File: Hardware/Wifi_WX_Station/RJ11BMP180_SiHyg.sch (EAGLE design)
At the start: 8 parts, among them U1 SI7021-DFN6

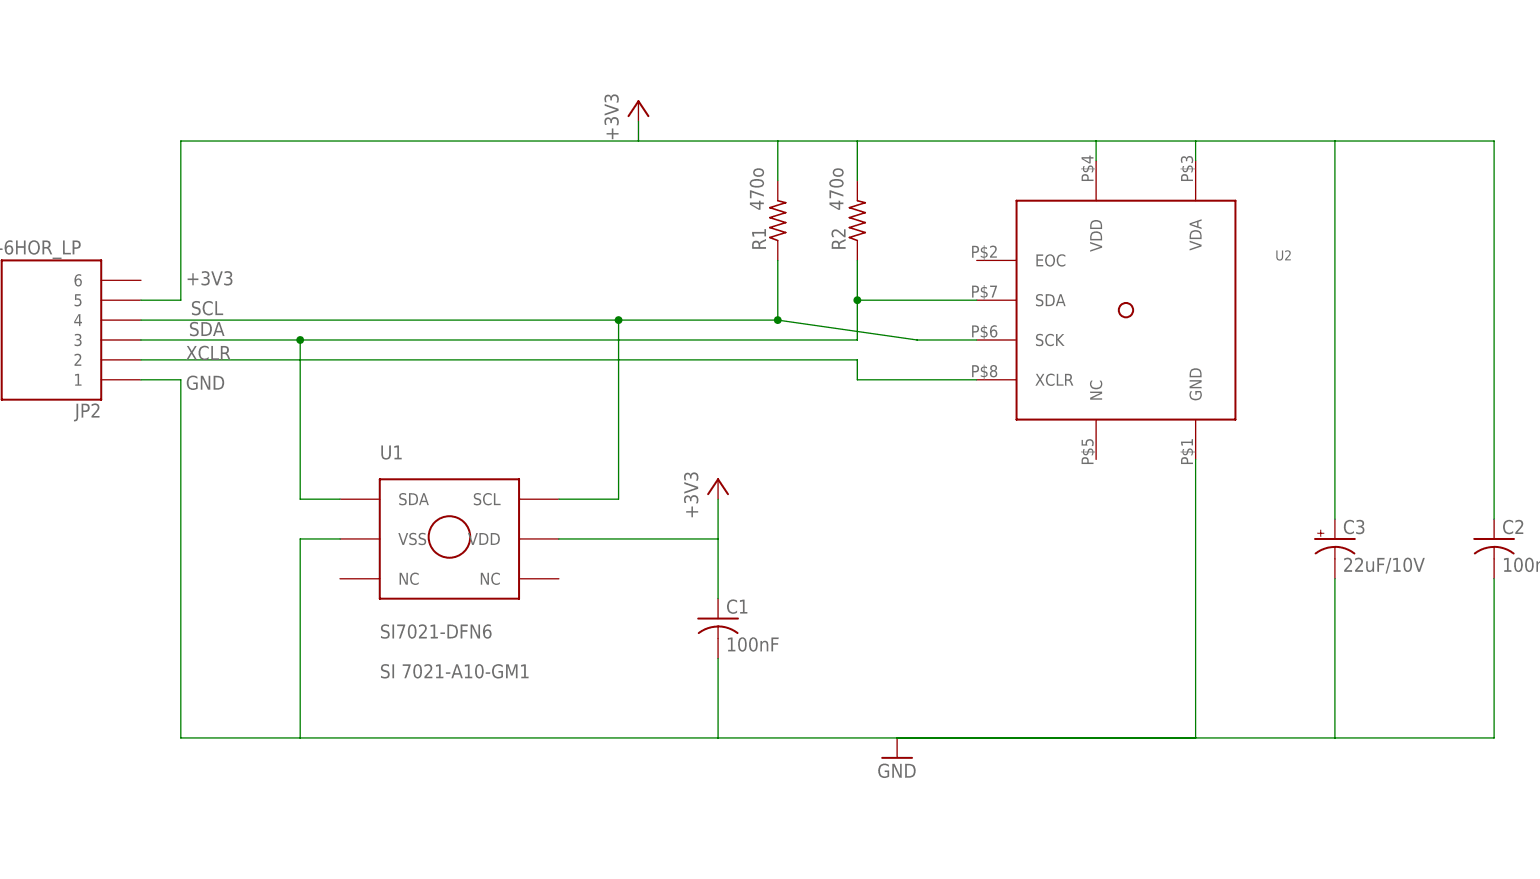
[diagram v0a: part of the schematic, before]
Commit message: added PCB for BOSH PMP180 revised WE28 schemaitc with added text
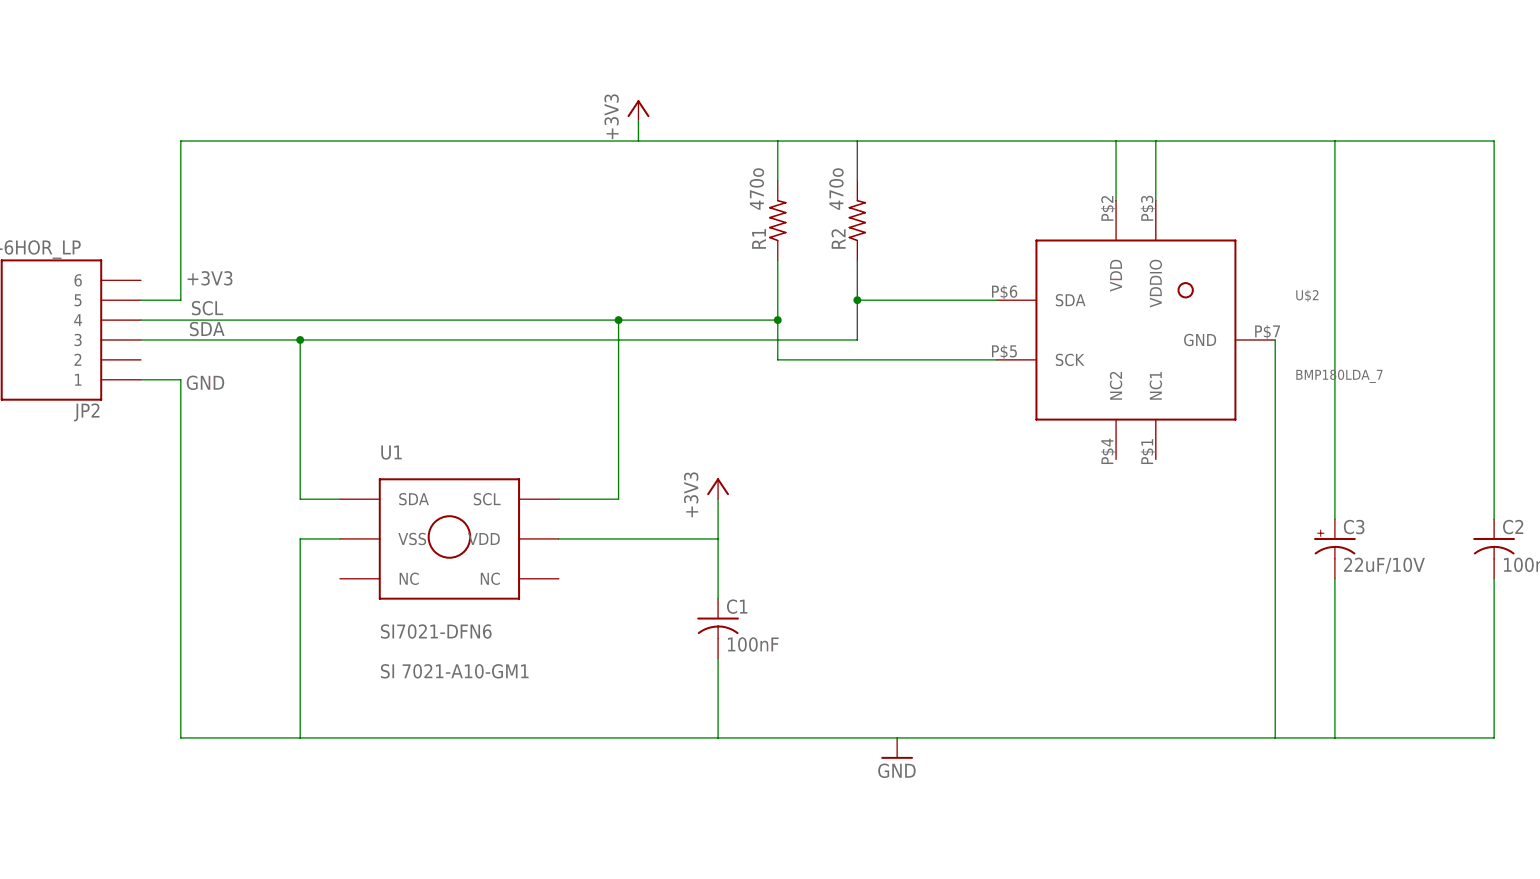
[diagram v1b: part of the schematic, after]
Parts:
- removed U2: (no value), 1AA_Stofer:BMP085
- added U$2: BMP180LDA_7, 1AA_Stofer:BMP180LDA_7
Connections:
- removed net XCLR: JP2.2, U2.XCLR
- net +3V3: now also U$2.VDD, U$2.VDDIO; no longer U2.VDA, U2.VDD
- net GND: now also U$2.GND; no longer U2.GND
- net SCL: now also U$2.SCK; no longer U2.SCK
- net SDA: now also U$2.SDA; no longer U2.SDA
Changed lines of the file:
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@@
 <part name="C3" library="rcl" deviceset="CPOL-US" device="SMCB" value="22uF/10V"/>
 <part name="C1" library="rcl" deviceset="C-US" device="C0805K" value="100nF"/>
-<part name="U2" library="1AA_Stofer" deviceset="BMP085" device=""/>
 <part name="JP2" library="wifi_WX" deviceset="RJ11-6" device="HOR_LP"/>
 <part name="U$1" library="1AA_Stofer" deviceset="8.5X11" device=""/>
 <part name="U1" library="wifi_WX" deviceset="SI7021" device="-DFN6"/>
 <part name="+3V2" library="supply1" deviceset="+3V3" device=""/>
+<part name="U$2" library="1AA_Stofer" deviceset="BMP180" device="LDA_7"/>
 </parts>
 <sheets>
@@
 <instance part="C3" gate="G$1" x="154.94" y="25.4"/>
 <instance part="C1" gate="G$1" x="76.2" y="15.24"/>
-<instance part="U2" gate="G$1" x="121.92" y="48.26"/>
 <instance part="JP2" gate="G$1" x="-7.62" y="55.88" rot="R180"/>
 <instance part="U$1" gate="G$1" x="-35.56" y="-58.42"/>
@@
 <instance part="U1" gate="G$1" x="33.02" y="17.78"/>
 <instance part="+3V2" gate="G$1" x="76.2" y="33.02"/>
+<instance part="U$2" gate="G$1" x="132.08" y="50.8"/>
 </instances>
 <busses>
@@
 <wire x1="22.86" y1="30.48" x2="22.86" y2="50.8" width="0.1524" layer="91"/>
 <junction x="22.86" y="50.8"/>
-<pinref part="U2" gate="G$1" pin="SDA"/>
-<wire x1="93.98" y1="55.88" x2="109.22" y2="55.88" width="0.1524" layer="91"/>
+<wire x1="93.98" y1="55.88" x2="111.76" y2="55.88" width="0.1524" layer="91"/>
 <junction x="93.98" y="55.88"/>
+<pinref part="U$2" gate="G$1" pin="SDA"/>
 </segment>
 </net>
@@
 <pinref part="R1" gate="G$1" pin="1"/>
 <wire x1="63.5" y1="53.34" x2="2.54" y2="53.34" width="0.1524" layer="91"/>
-<wire x1="83.82" y1="53.34" x2="101.6" y2="50.8" width="0.1524" layer="91"/>
-<pinref part="U2" gate="G$1" pin="SCK"/>
-<wire x1="101.6" y1="50.8" x2="109.22" y2="50.8" width="0.1524" layer="91"/>
+<wire x1="83.82" y1="53.34" x2="83.82" y2="48.26" width="0.1524" layer="91"/>
+<wire x1="83.82" y1="48.26" x2="111.76" y2="48.26" width="0.1524" layer="91"/>
 <pinref part="JP2" gate="G$1" pin="4"/>
 <pinref part="U1" gate="G$1" pin="SCL"/>
@@
 <wire x1="63.5" y1="30.48" x2="63.5" y2="53.34" width="0.1524" layer="91"/>
 <junction x="63.5" y="53.34"/>
+<pinref part="U$2" gate="G$1" pin="SCK"/>
 </segment>
 </net>
@@
 <wire x1="76.2" y1="10.16" x2="76.2" y2="0" width="0.1524" layer="91"/>
 <pinref part="C1" gate="G$1" pin="2"/>
-<pinref part="U2" gate="G$1" pin="GND"/>
-<wire x1="137.16" y1="35.56" x2="137.16" y2="0" width="0.1524" layer="91"/>
-<wire x1="137.16" y1="0" x2="99.06" y2="0" width="0.1524" layer="91"/>
+<wire x1="147.32" y1="50.8" x2="147.32" y2="0" width="0.1524" layer="91"/>
 <pinref part="C3" gate="G$1" pin="-"/>
 <wire x1="154.94" y1="20.32" x2="154.94" y2="0" width="0.1524" layer="91"/>
@@
 <wire x1="175.26" y1="0" x2="154.94" y2="0" width="0.1524" layer="91"/>
 <pinref part="JP2" gate="G$1" pin="1"/>
-<wire x1="154.94" y1="0" x2="99.06" y2="0" width="0.1524" layer="91"/>
+<wire x1="154.94" y1="0" x2="147.32" y2="0" width="0.1524" layer="91"/>
+<wire x1="147.32" y1="0" x2="99.06" y2="0" width="0.1524" layer="91"/>
 <wire x1="2.54" y1="45.72" x2="7.62" y2="45.72" width="0.1524" layer="91"/>
 <pinref part="U1" gate="G$1" pin="VSS"/>
 <wire x1="27.94" y1="25.4" x2="22.86" y2="25.4" width="0.1524" layer="91"/>
 <wire x1="22.86" y1="25.4" x2="22.86" y2="0" width="0.1524" layer="91"/>
+<pinref part="U$2" gate="G$1" pin="GND"/>
 </segment>
 </net>
@@
 <segment>
 <wire x1="83.82" y1="76.2" x2="93.98" y2="76.2" width="0.1524" layer="91"/>
-<wire x1="93.98" y1="76.2" x2="124.46" y2="76.2" width="0.1524" layer="91"/>
-<wire x1="124.46" y1="76.2" x2="137.16" y2="76.2" width="0.1524" layer="91"/>
+<wire x1="93.98" y1="76.2" x2="127" y2="76.2" width="0.1524" layer="91"/>
+<wire x1="127" y1="76.2" x2="132.08" y2="76.2" width="0.1524" layer="91"/>
 <wire x1="83.82" y1="71.12" x2="83.82" y2="76.2" width="0.1524" layer="91"/>
 <wire x1="83.82" y1="76.2" x2="66.04" y2="76.2" width="0.1524" layer="91"/>
@@
 <pinref part="R1" gate="G$1" pin="2"/>
 <pinref part="+3V1" gate="G$1" pin="+3V3"/>
-<wire x1="154.94" y1="76.2" x2="137.16" y2="76.2" width="0.1524" layer="91"/>
-<pinref part="U2" gate="G$1" pin="VDD"/>
-<wire x1="124.46" y1="73.66" x2="124.46" y2="76.2" width="0.1524" layer="91"/>
-<pinref part="U2" gate="G$1" pin="VDA"/>
-<wire x1="137.16" y1="73.66" x2="137.16" y2="76.2" width="0.1524" layer="91"/>
+<wire x1="154.94" y1="76.2" x2="132.08" y2="76.2" width="0.1524" layer="91"/>
+<wire x1="127" y1="68.58" x2="127" y2="76.2" width="0.1524" layer="91"/>
+<wire x1="132.08" y1="68.58" x2="132.08" y2="76.2" width="0.1524" layer="91"/>
 <pinref part="C2" gate="G$1" pin="1"/>
 <pinref part="C3" gate="G$1" pin="+"/>
@@
 <pinref part="R2" gate="G$1" pin="2"/>
 <wire x1="93.98" y1="71.12" x2="93.98" y2="76.2" width="0.1524" layer="91"/>
+<pinref part="U$2" gate="G$1" pin="VDD"/>
+<pinref part="U$2" gate="G$1" pin="VDDIO"/>
 </segment>
 <segment>
@@
 </segment>
 </net>
-<net name="XCLR" class="0">
-<segment>
-<wire x1="93.98" y1="48.26" x2="2.54" y2="48.26" width="0.1524" layer="91"/>
-<label x="8.255" y="48.26" size="1.778" layer="95"/>
-<wire x1="93.98" y1="48.26" x2="93.98" y2="45.72" width="0.1524" layer="91"/>
-<pinref part="U2" gate="G$1" pin="XCLR"/>
-<wire x1="93.98" y1="45.72" x2="109.22" y2="45.72" width="0.1524" layer="91"/>
-<pinref part="JP2" gate="G$1" pin="2"/>
-</segment>
-</net>
